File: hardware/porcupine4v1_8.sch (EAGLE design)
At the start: 33 parts, among them X1 PROGCON

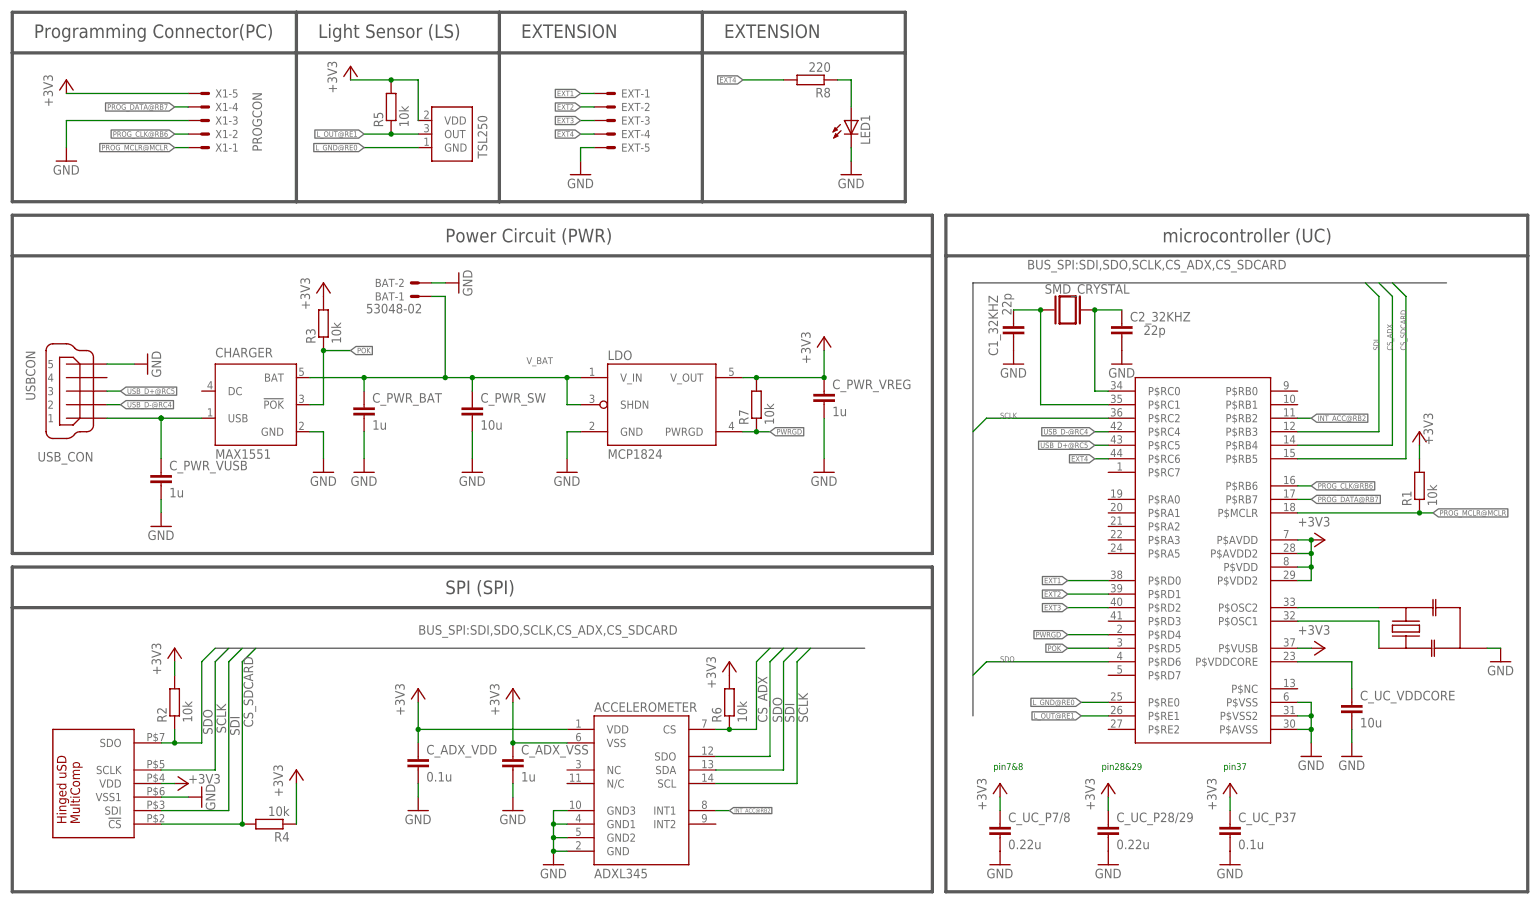
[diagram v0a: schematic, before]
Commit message: updated porcupine4v1_8: fixed 12MHZ resonator board footprint
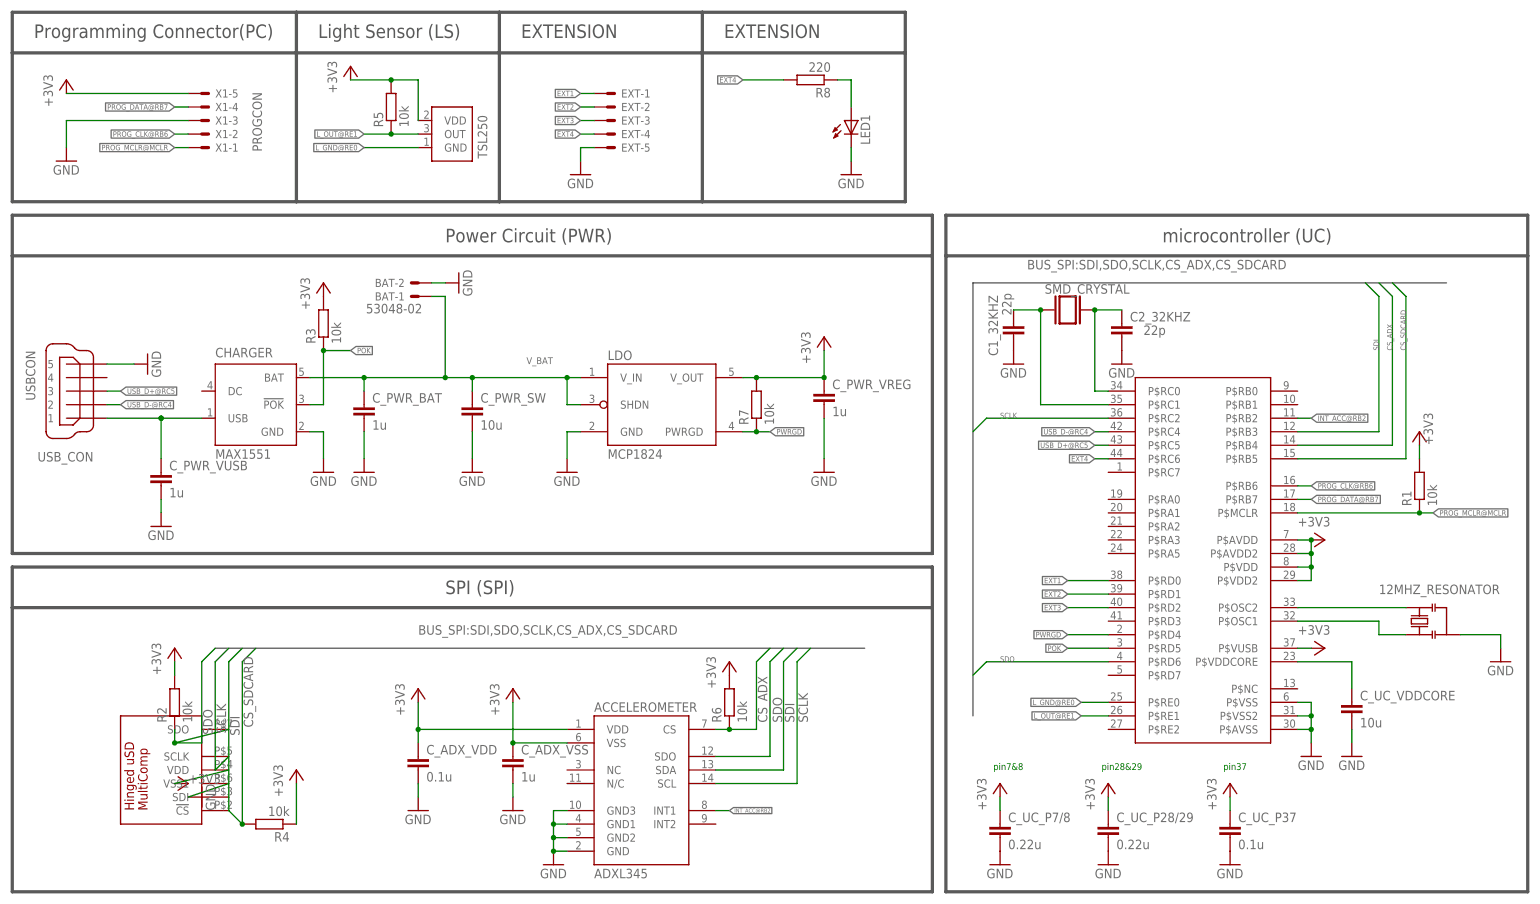
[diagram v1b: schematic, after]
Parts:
- 12MHZ_RESONATOR: value RESONATORPRQC-S -> RESONATORPRQC-C; device jnode:RESONATORPRQC-S -> HedgehogLib:RESONATORPRQC-C; DIGIKEY http://www.digikey.com/product-detail/en/PRQC12.00CR5010X00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 -> (none)
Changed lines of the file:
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@@
 <part name="R3" library="rcl" deviceset="R-EU_" device="R0603" value="10k"/>
 <part name="R5" library="rcl" deviceset="R-EU_" device="R0603" value="10k"/>
-<part name="12MHZ_RESONATOR" library="jnode" deviceset="RESONATOR" device="PRQC-S">
-<attribute name="DIGIKEY" value="http://www.digikey.com/product-detail/en/PRQC12.00CR5010X000/478-6318-1-ND/2506334"/>
-</part>
 <part name="GND1" library="supply1" deviceset="GND" device=""/>
 <part name="32KHZ_CRYSTAL" library="HedgehogLib" deviceset="SMD_CRYSTAL" device=""/>
@@
 <part name="LED1" library="led" deviceset="LED" device="SML0805"/>
 <part name="GND10" library="supply1" deviceset="GND" device=""/>
+<part name="12MHZ_RESONATOR" library="HedgehogLib" deviceset="RESONATOR" device="PRQC-C"/>
 </parts>
 <sheets>
@@
 <instance part="R3" gate="G$1" x="60.96" y="109.22" rot="R90"/>
 <instance part="R5" gate="G$1" x="73.66" y="149.86" rot="R90"/>
-<instance part="12MHZ_RESONATOR" gate="G$1" x="266.7" y="50.8" rot="R180"/>
 <instance part="GND1" gate="1" x="281.94" y="45.72"/>
 <instance part="32KHZ_CRYSTAL" gate="G$1" x="200.66" y="111.76" smashed="yes">
@@
 <instance part="LED1" gate="G$1" x="160.02" y="147.32"/>
 <instance part="GND10" gate="1" x="109.22" y="137.16"/>
+<instance part="12MHZ_RESONATOR" gate="RESONATOR" x="266.7" y="53.34" smashed="yes" rot="R180">
+<attribute name="NAME" x="259.08" y="58.42" size="1.778" layer="95"/>
+</instance>
 </instances>
 <busses>
@@
 </segment>
 <segment>
-<wire x1="30.48" y1="20.32" x2="35.56" y2="20.32" width="0.1524" layer="91"/>
+<wire x1="43.18" y1="22.86" x2="35.56" y2="20.32" width="0.1524" layer="91"/>
 <pinref part="SDCARD_CON" gate="G$1" pin="VSS1"/>
 <pinref part="GND16" gate="1" pin="GND"/>
@@
 </segment>
 <segment>
-<pinref part="12MHZ_RESONATOR" gate="G$1" pin="GND"/>
 <pinref part="GND1" gate="1" pin="GND"/>
-<wire x1="279.4" y1="48.26" x2="281.94" y2="48.26" width="0.1524" layer="91"/>
+<pinref part="12MHZ_RESONATOR" gate="RESONATOR" pin="GND"/>
+<wire x1="274.32" y1="50.8" x2="281.94" y2="50.8" width="0.1524" layer="91"/>
+<wire x1="281.94" y1="50.8" x2="281.94" y2="48.26" width="0.1524" layer="91"/>
 </segment>
 <segment>
@@
 </segment>
 <segment>
-<wire x1="33.02" y1="22.86" x2="30.48" y2="22.86" width="0.1524" layer="91"/>
+<wire x1="33.02" y1="22.86" x2="43.18" y2="25.4" width="0.1524" layer="91"/>
 <pinref part="SDCARD_CON" gate="G$1" pin="VDD"/>
 <pinref part="+3V2" gate="G$1" pin="+3V3"/>
@@
 </segment>
 <segment>
-<wire x1="30.48" y1="17.78" x2="43.18" y2="17.78" width="0.1524" layer="91"/>
-<wire x1="43.18" y1="17.78" x2="43.18" y2="45.72" width="0.1524" layer="91"/>
+<wire x1="43.18" y1="20.32" x2="43.18" y2="17.78" width="0.1524" layer="91"/>
+<wire x1="43.18" y1="20.32" x2="43.18" y2="45.72" width="0.1524" layer="91"/>
 <wire x1="43.18" y1="45.72" x2="45.72" y2="48.26" width="0.1524" layer="91"/>
 <label x="43.434" y="35.56" size="1.778" layer="95" rot="R270"/>
@@
 <wire x1="38.1" y1="30.48" x2="38.1" y2="45.72" width="0.1524" layer="91"/>
 <wire x1="38.1" y1="45.72" x2="40.64" y2="48.26" width="0.1524" layer="91"/>
-<wire x1="30.48" y1="30.48" x2="33.02" y2="30.48" width="0.1524" layer="91"/>
+<wire x1="43.18" y1="33.02" x2="33.02" y2="30.48" width="0.1524" layer="91"/>
 <wire x1="33.02" y1="33.02" x2="33.02" y2="30.48" width="0.1524" layer="91"/>
 <wire x1="33.02" y1="30.48" x2="38.1" y2="30.48" width="0.1524" layer="91"/>
@@
 </segment>
 <segment>
-<wire x1="30.48" y1="25.4" x2="40.64" y2="25.4" width="0.1524" layer="91"/>
+<wire x1="43.18" y1="27.94" x2="40.64" y2="25.4" width="0.1524" layer="91"/>
 <wire x1="40.64" y1="25.4" x2="40.64" y2="45.72" width="0.1524" layer="91"/>
 <wire x1="40.64" y1="45.72" x2="43.18" y2="48.26" width="0.1524" layer="91"/>
@@
 <net name="CS_SDCARD" class="0">
 <segment>
-<wire x1="30.48" y1="15.24" x2="45.72" y2="15.24" width="0.1524" layer="91"/>
+<wire x1="43.18" y1="17.78" x2="45.72" y2="15.24" width="0.1524" layer="91"/>
 <wire x1="45.72" y1="15.24" x2="45.72" y2="45.72" width="0.1524" layer="91"/>
 <wire x1="45.72" y1="45.72" x2="48.26" y2="48.26" width="0.1524" layer="91"/>
@@
 <segment>
 <pinref part="PIC_CONTROLLER" gate="G$1" pin="P$OSC1"/>
-<pinref part="12MHZ_RESONATOR" gate="G$1" pin="2"/>
 <wire x1="243.84" y1="53.34" x2="259.08" y2="53.34" width="0.1524" layer="91"/>
-<wire x1="259.08" y1="53.34" x2="259.08" y2="48.26" width="0.1524" layer="91"/>
+<wire x1="259.08" y1="53.34" x2="259.08" y2="50.8" width="0.1524" layer="91"/>
+<wire x1="259.08" y1="50.8" x2="264.16" y2="50.8" width="0.1524" layer="91"/>
+<pinref part="12MHZ_RESONATOR" gate="RESONATOR" pin="2"/>
 </segment>
 </net>
@@
 <segment>
 <pinref part="PIC_CONTROLLER" gate="G$1" pin="P$OSC2"/>
-<pinref part="12MHZ_RESONATOR" gate="G$1" pin="1"/>
-<wire x1="243.84" y1="55.88" x2="259.08" y2="55.88" width="0.1524" layer="91"/>
-</segment>
-</net>
+<wire x1="243.84" y1="55.88" x2="264.16" y2="55.88" width="0.1524" layer="91"/>
+<pinref part="12MHZ_RESONATOR" gate="RESONATOR" pin="1"/>
+</segment>
+</net>
